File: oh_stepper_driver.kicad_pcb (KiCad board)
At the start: 4 copper layers, 55.9 x 43.2 mm, 47 parts, among them J1 JTAG, P1 CONN_01X04, P2 CONN_01X02, P3 CONN_01X02, Q1 CSD18531Q5A, Q2 CSD18531Q5A, Q3 CSD18531Q5A, Q4 CSD18531Q5A, Q5 CSD18531Q5A, Q6 CSD18531Q5A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

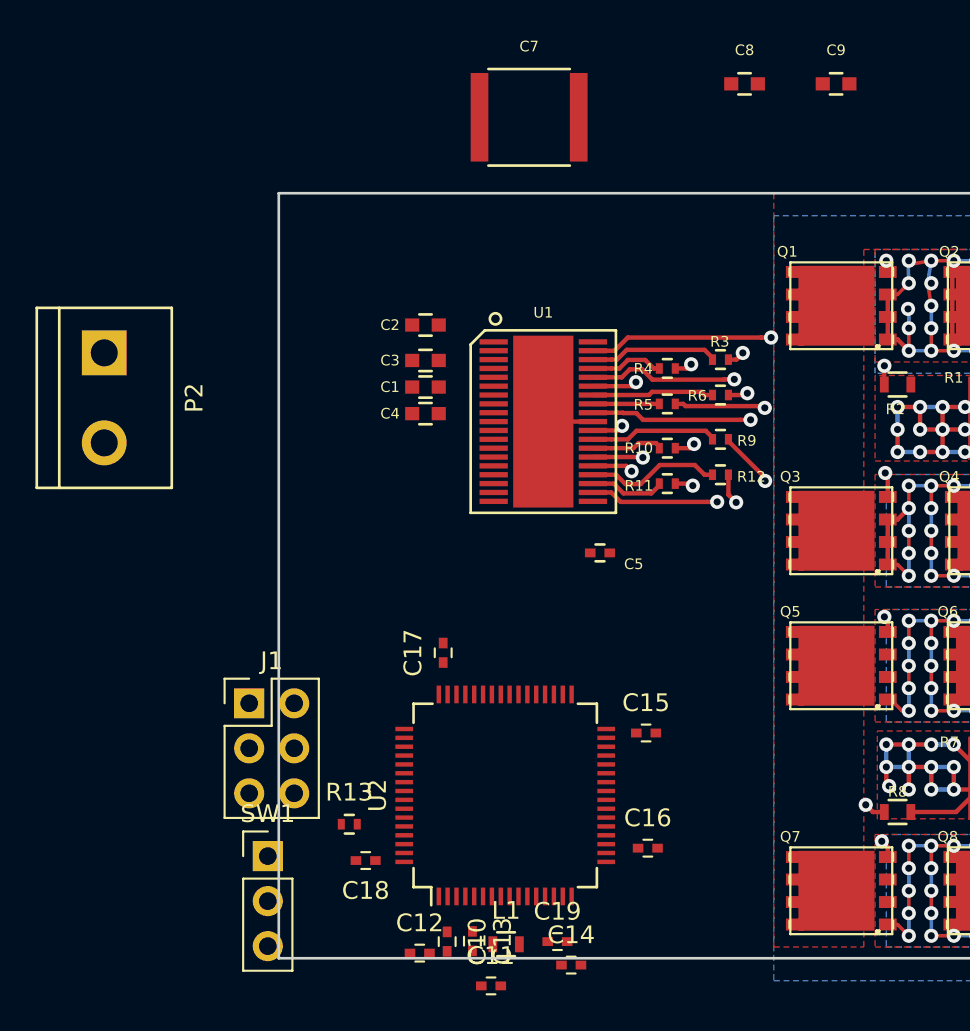
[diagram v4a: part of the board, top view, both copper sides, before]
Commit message: library of transeiver can
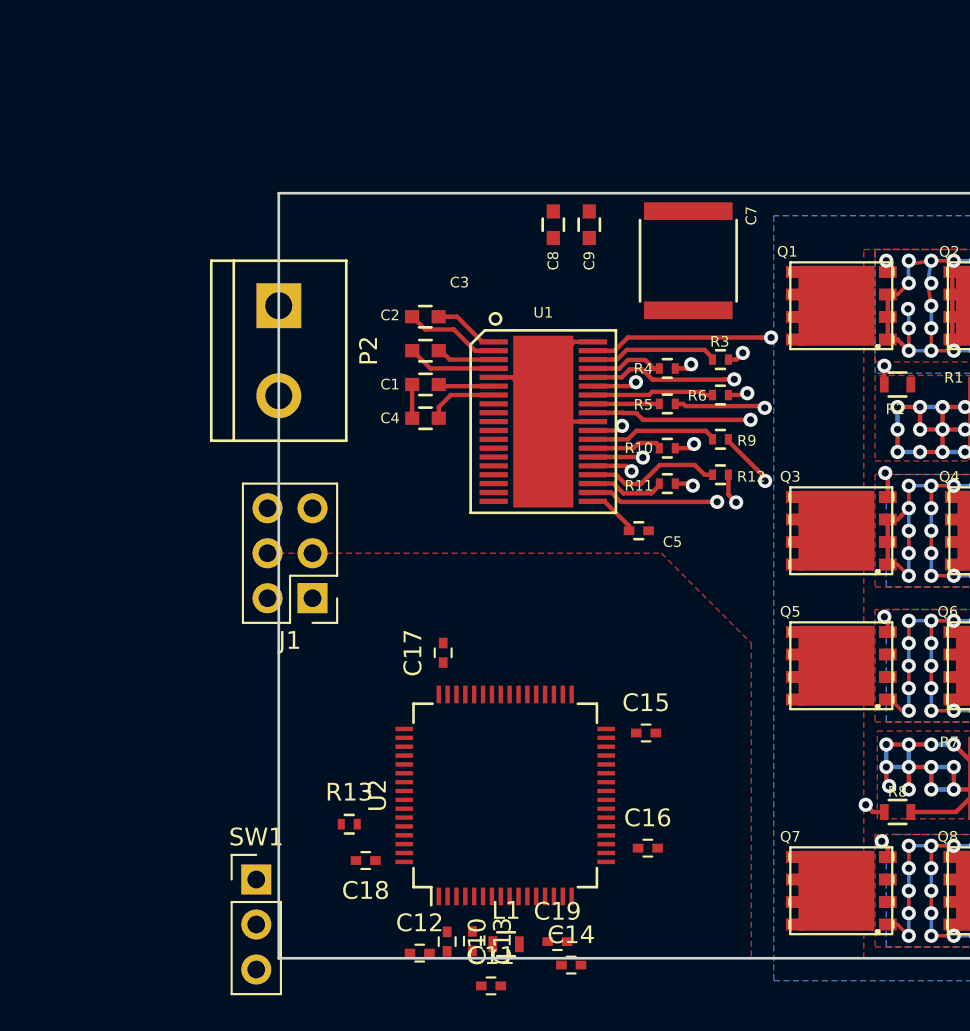
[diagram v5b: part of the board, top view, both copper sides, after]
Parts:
- moved C9 16.0 mm to (133.1, 56.4), turned to 90 degrees
- moved C8 13.4 mm to (131.1, 56.4), turned to 90 degrees
- moved C7 12.1 mm to (138.7, 58.4), turned to 90 degrees
- moved P2 10.2 mm to (115.6, 63.5)
- moved J1 6.92 mm to (117.5, 77.5), turned to 180 degrees
- moved C5 2.52 mm to (135.9, 73.7)
- moved SW1 1.47 mm to (114.3, 93.3)
- moved C2 0.55 mm to (123.8, 63.5)
- moved C3 0.47 mm to (123.8, 61.6)
- moved C4 0.26 mm to (123.8, 67.3)
- moved C1 0.14 mm to (123.8, 65.4)
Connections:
- C7 pad 1: Net-(C7-Pad1) -> VM
- C7 pad 2: Net-(C7-Pad2) -> GND
- C8 pad 1: Net-(C7-Pad1) -> VM
- C8 pad 2: Net-(C7-Pad2) -> GND
- C9 pad 1: Net-(C7-Pad1) -> VM
- C9 pad 2: Net-(C7-Pad2) -> GND
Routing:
- net GND: track 48.5 -> 61.0 mm
- net Net-(C3-Pad2): track 0.00 -> 5.41 mm
- net VM: track 0.00 -> 5.01 mm
- net Net-(C4-Pad1): track 0.00 -> 4.01 mm
- net Net-(C3-Pad1): track 0.00 -> 3.70 mm
- net Net-(C2-Pad2): track 0.00 -> 3.31 mm
- net Net-(C1-Pad1): track 0.00 -> 3.14 mm
- net Net-(C5-Pad1): track 0.00 -> 2.89 mm

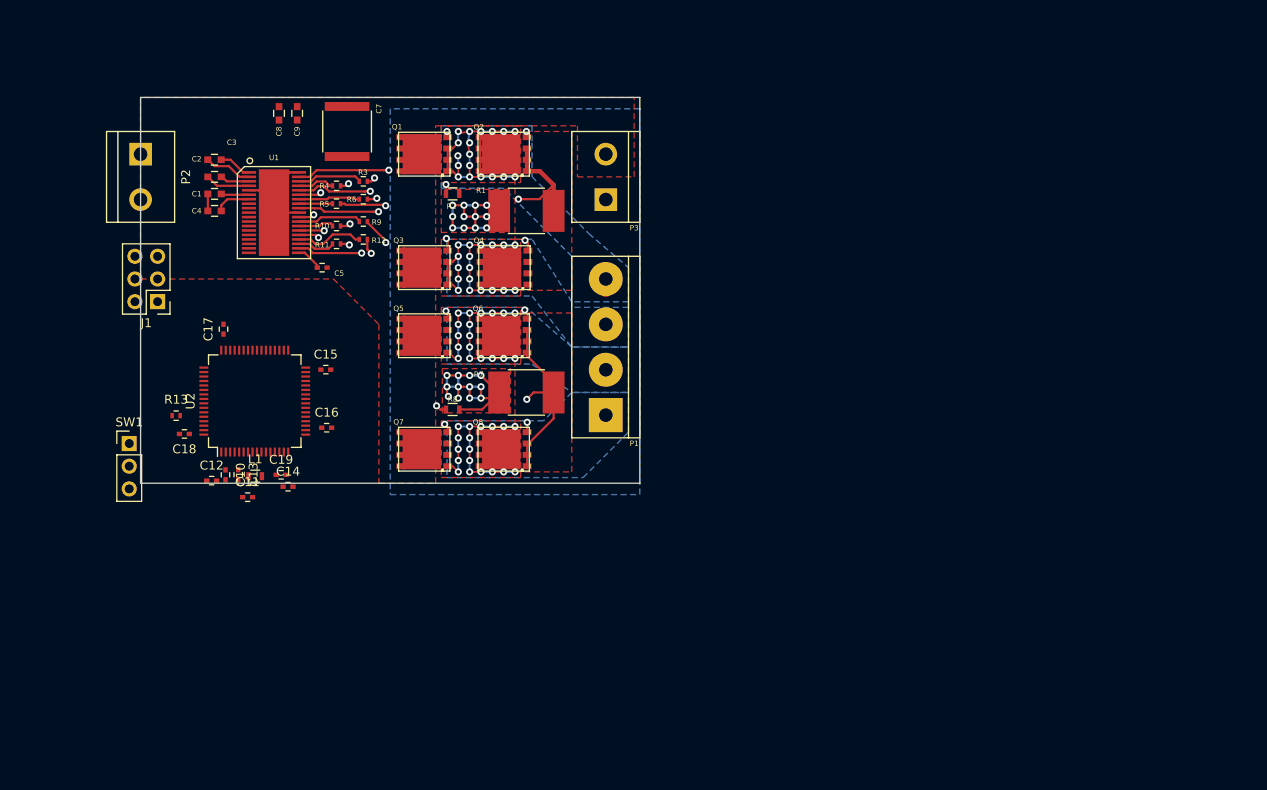
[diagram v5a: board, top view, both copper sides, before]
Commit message: encoder placement
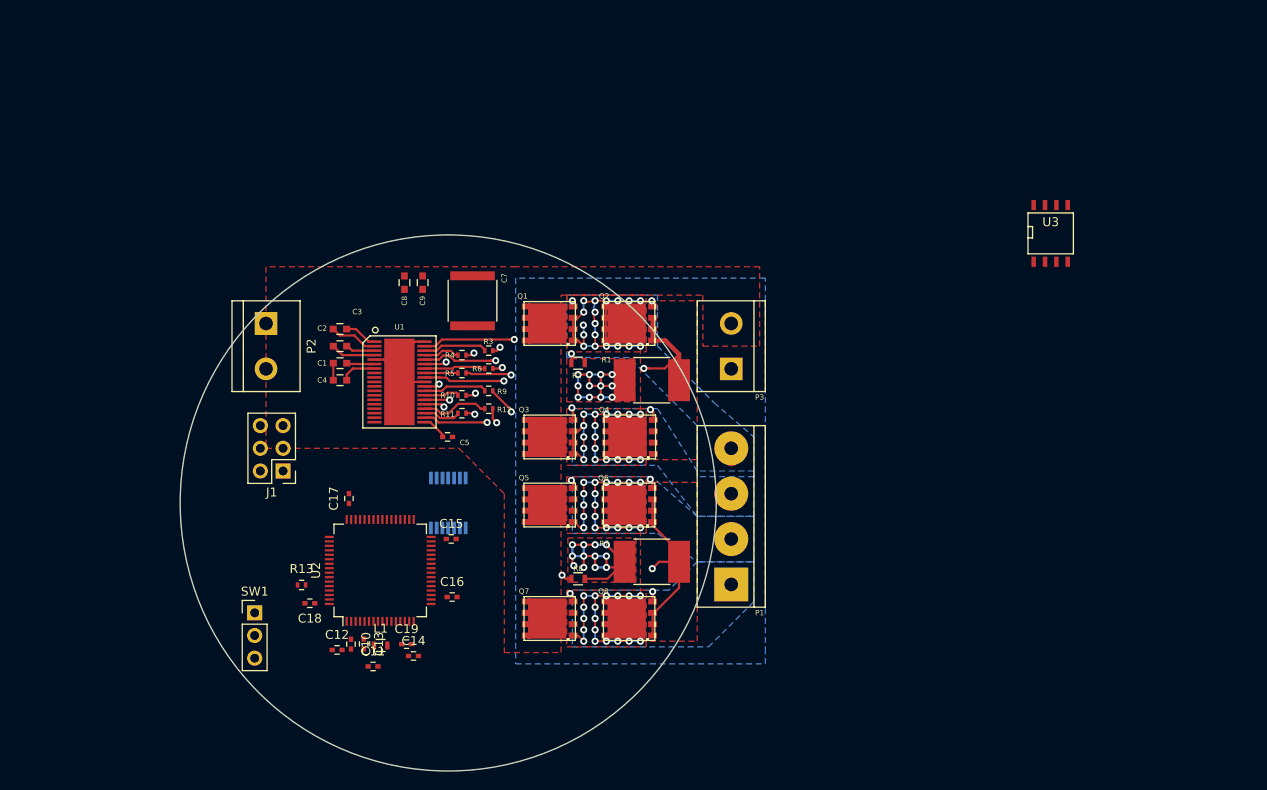
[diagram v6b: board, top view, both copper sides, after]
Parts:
- added U3: TJA1050, SMD_Packages:SOIC-8-N, F.Cu at (217.4, 69.8)
- added U4: AS5047D, SMD_Packages:SSOP-14, B.Cu at (150.0, 100.0)
- moved C14 23.6 mm to (146.1, 117.1)
- moved C5 23.6 mm to (149.9, 92.6)
- moved P1 23.6 mm to (181.7, 101.5)
- moved P2 23.6 mm to (129.6, 82.5)
- moved P3 23.6 mm to (181.7, 82.5)
- moved Q3 23.6 mm to (161.4, 92.6)
- moved Q4 23.6 mm to (170.3, 92.6)
- moved Q5 23.6 mm to (161.4, 100.2)
- moved Q7 23.6 mm to (161.4, 112.9)
- moved C8 23.6 mm to (145.1, 75.3)
- moved Q1 23.6 mm to (161.4, 79.9)
- moved C10 23.6 mm to (139.1, 115.8)
- moved C11 23.6 mm to (141.6, 118.3)
- moved R13 23.6 mm to (133.6, 109.2)
- moved SW1 23.6 mm to (128.3, 112.3)
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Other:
- board size 55.9 x 43.2 mm -> 60 x 60 mm
